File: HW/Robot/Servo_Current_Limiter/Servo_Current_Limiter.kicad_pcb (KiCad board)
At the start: 2 copper layers, 19 parts, among them J1 1x1 2.54mm male, J11 1x2 2.54mm male, J2 1x5 2.54mm male, J3 1x1 2.54mm male, Q1 IRF4905, Q2 BC338, U1 TL071

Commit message: Sch update.
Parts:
- removed C2: 100n, For_Rasterboard:C_Disc_D3.0mm_W1.6mm_Pinf
- added J10: 1x3 2.54mm male, Connector_PinHeader_2.54mm:PinHeader_1x03_P2.54mm_Vertical, F.Cu at (170.4, 50.4)
- added J11: 1x1 2.54mm male, Connector_PinHeader_2.54mm:PinHeader_1x01_P2.54mm_Vertical, F.Cu at (240.0, 28.4)
- added J12: 1x1 2.54mm male, Connector_PinHeader_2.54mm:PinHeader_1x01_P2.54mm_Vertical, F.Cu at (169.0, 38.1)
- added J13: 1x3 2.54mm male, Connector_PinHeader_2.54mm:PinHeader_1x03_P2.54mm_Vertical, F.Cu at (170.4, 28.4)
- added J14: 1x1 2.54mm male, Connector_PinHeader_2.54mm:PinHeader_1x01_P2.54mm_Vertical, F.Cu at (203.3, 50.4)
- added J4: 1x3 2.54mm male, Connector_PinHeader_2.54mm:PinHeader_1x03_P2.54mm_Vertical, F.Cu at (188.0, 139.7)
- added J6: 1x1 2.54mm male, Connector_PinHeader_2.54mm:PinHeader_1x01_P2.54mm_Vertical, F.Cu at (205.7, 38.1)
- added J7: 1x3 2.54mm male, Connector_PinHeader_2.54mm:PinHeader_1x03_P2.54mm_Vertical, F.Cu at (207.2, 28.4)
- added J8: 1x1 2.54mm male, Connector_PinHeader_2.54mm:PinHeader_1x01_P2.54mm_Vertical, F.Cu at (238.5, 53.5)
- added J9: 1x1 2.54mm male, Connector_PinHeader_2.54mm:PinHeader_1x01_P2.54mm_Vertical, F.Cu at (169.0, 60.1)
- added JP1: 1x2 2.54mm male, Connector_PinHeader_2.54mm:PinHeader_1x02_P2.54mm_Vertical, F.Cu at (119.4, 129.5)
- added Q3: IRF4905, Package_TO_SOT_THT:TO-220-3_Vertical, F.Cu at (196.5, 30.0)
- added Q4: BC338, For_Rasterboard:TO-92_Inline_inf, F.Cu at (194.8, 35.3)
- added Q5: IRF4905, Package_TO_SOT_THT:TO-220-3_Vertical, F.Cu at (159.8, 52.0)
- added Q6: BC338, For_Rasterboard:TO-92_Inline_inf, F.Cu at (158.1, 57.3)
- added Q7: IRF4905, Package_TO_SOT_THT:TO-220-3_Vertical, F.Cu at (159.8, 30.0)
- added Q8: BC338, For_Rasterboard:TO-92_Inline_inf, F.Cu at (158.1, 35.3)
- added R10: 10k, For_Rasterboard:R_Axial_DIN0207_L6.3mm_D2.5mm_P7.62mm_Horizontal, F.Cu at (227.0, 65.3)
- added R11: 10k, For_Rasterboard:R_Axial_DIN0207_L6.3mm_D2.5mm_P7.62mm_Horizontal, F.Cu at (227.0, 53.2)
- added R12: 100k, For_Rasterboard:R_Axial_DIN0207_L6.3mm_D2.5mm_P2.54mm_Vertical, F.Cu at (227.0, 57.2)
- added R13: 220, For_Rasterboard:R_Axial_DIN0207_L6.3mm_D2.5mm_Pinf_Horizontal, F.Cu at (157.5, 61.9)
- added R14: 0.1, Resistor_THT:R_Axial_DIN0207_L6.3mm_D2.5mm_P10.16mm_Horizontal, F.Cu at (144.2, 61.9)
- added R15: 100k, For_Rasterboard:R_Axial_DIN0207_L6.3mm_D2.5mm_Pinf_Horizontal, F.Cu at (228.5, 36.2)
- added R16: 10k, For_Rasterboard:R_Axial_DIN0207_L6.3mm_D2.5mm_P7.62mm_Horizontal, F.Cu at (228.5, 40.2)
- added R17: 10k, For_Rasterboard:R_Axial_DIN0207_L6.3mm_D2.5mm_P7.62mm_Horizontal, F.Cu at (228.5, 28.1)
- added R18: 100k, For_Rasterboard:R_Axial_DIN0207_L6.3mm_D2.5mm_P2.54mm_Vertical, F.Cu at (228.5, 32.1)
- added R19: 220, For_Rasterboard:R_Axial_DIN0207_L6.3mm_D2.5mm_Pinf_Horizontal, F.Cu at (157.5, 40.0)
- added R20: 0.1, Resistor_THT:R_Axial_DIN0207_L6.3mm_D2.5mm_P10.16mm_Horizontal, F.Cu at (144.2, 40.0)
- added R21: 100k, For_Rasterboard:R_Axial_DIN0207_L6.3mm_D2.5mm_Pinf_Horizontal, F.Cu at (191.8, 58.2)
- added R22: 10k, For_Rasterboard:R_Axial_DIN0207_L6.3mm_D2.5mm_P7.62mm_Horizontal, F.Cu at (191.8, 62.2)
- added R23: 10k, For_Rasterboard:R_Axial_DIN0207_L6.3mm_D2.5mm_P7.62mm_Horizontal, F.Cu at (191.8, 50.1)
- added R24: 100k, For_Rasterboard:R_Axial_DIN0207_L6.3mm_D2.5mm_P2.54mm_Vertical, F.Cu at (191.8, 54.1)
- added R8: 0.1, Resistor_THT:R_Axial_DIN0207_L6.3mm_D2.5mm_P10.16mm_Horizontal, F.Cu at (180.9, 40.0)
- added R9: 100k, For_Rasterboard:R_Axial_DIN0207_L6.3mm_D2.5mm_Pinf_Horizontal, F.Cu at (227.0, 61.3)
- added RV3: 250, Potentiometer_THT:Potentiometer_Piher_PT-10-V10_Vertical, F.Cu at (144.6, 56.6)
- added RV4: 250, Potentiometer_THT:Potentiometer_Piher_PT-10-V10_Vertical, F.Cu at (144.6, 34.6)
- C1: footprint For_Rasterboard:C_Disc_D3.0mm_W1.6mm_Pinf -> For_Rasterboard:C_Disc_D3.0mm_W1.6mm_P5.00mm
- J2: value 1x5 2.54mm male -> Conn_02x05_Odd_Even; footprint Connector_PinSocket_2.54mm:PinSocket_1x05_P2.54mm_Vertical -> Connector_PinSocket_2.54mm:PinSocket_2x05_P2.54mm_Vertical
- R3: value 220k -> 100k; footprint For_Rasterboard:R_Axial_DIN0207_L6.3mm_D2.5mm_Pinf_Horizontal -> For_Rasterboard:R_Axial_DIN0207_L6.3mm_D2.5mm_P7.62mm_Horizontal
- R4: value 220k -> 10k; footprint For_Rasterboard:R_Axial_DIN0207_L6.3mm_D2.5mm_P7.62mm_Horizontal -> For_Rasterboard:R_Axial_DIN0207_L6.3mm_D2.5mm_P5.08mm_Vertical
- R5: value 220k -> 10k
- R6: value 220k -> 100k; footprint For_Rasterboard:R_Axial_DIN0207_L6.3mm_D2.5mm_Pinf_Horizontal -> For_Rasterboard:R_Axial_DIN0207_L6.3mm_D2.5mm_P2.54mm_Vertical
- R7: value 1k5 -> 220; footprint For_Rasterboard:R_Axial_DIN0207_L6.3mm_D2.5mm_P5.08mm_Vertical -> For_Rasterboard:R_Axial_DIN0207_L6.3mm_D2.5mm_Pinf_Horizontal
- RV2: value 100k -> 250; footprint Potentiometer_THT:Potentiometer_Piher_PT-10-H01_Horizontal -> Potentiometer_THT:Potentiometer_Piher_PT-10-V10_Vertical
- U1: value TL071 -> LM324; footprint Package_DIP:DIP-8_W7.62mm -> Package_DIP:DIP-14_W7.62mm
- moved J2 125.3 mm to (33.0, 162.6)
- moved R7 75.3 mm to (194.2, 40.0)
- moved C1 69.7 mm to (139.7, 139.7)
- moved RV2 68.9 mm to (181.3, 34.6)
- moved U1 46.5 mm to (210.8, 142.2)
- moved Q1 43.4 mm to (193.0, 134.6), turned to -90 degrees
- moved RV1 38.6 mm to (177.8, 132.0)
- moved Q2 35.7 mm to (182.9, 137.2), turned to 90 degrees
- moved R1 34.6 mm to (175.3, 142.2), turned to 90 degrees
- moved R5 31.3 mm to (200.7, 144.8), turned to 90 degrees
- moved R6 30.9 mm to (205.7, 142.2), turned to -90 degrees
- moved R2 26.3 mm to (165.1, 129.5), turned to -90 degrees
- moved R3 22.2 mm to (203.2, 139.7), turned to -90 degrees
- moved R4 20.2 mm to (195.6, 142.2), turned to -90 degrees
- moved J5 17.7 mm to (198.1, 142.2)
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- renumbered J11 to J1, J1 to J3, J3 to J5
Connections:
- net /ch0/sub/op/IN+ renamed Net-(R3-Pad2)
- net /ch0/sub/op/IN- renamed Net-(R5-Pad1)
- A1 pad 10: unconnected-(A1-Pad10) -> /OUT1
- A1 pad 11: unconnected-(A1-Pad11) -> /OUT2
- A1 pad 12: unconnected-(A1-Pad12) -> /OUT3
- A1 pad 17: /DIS0 -> unconnected-(A1-Pad17)
- A1 pad 20: unconnected-(A1-Pad20) -> /ARD_PWM3
- A1 pad 24: unconnected-(A1-Pad24) -> /ARD_PWM2
- A1 pad 25: unconnected-(A1-Pad25) -> /ARD_PWM1
- A1 pad 26: unconnected-(A1-Pad26) -> /ARD_PWM0
- A1 pad 5: +5V -> Net-(A1-Pad5)
- C1 pad 2: GNDA -> GND
- J2 pad 1: unconnected-(J2-Pad1) -> /ARD_PWM0
- J2 pad 2: unconnected-(J2-Pad2) -> /PWM0
- J2 pad 3: /ch0/PWM -> /ARD_PWM1
- J2 pad 4: /ch0/N -> /PWM1
- J2 pad 5: GND -> /ARD_PWM2
- R3 pad 1: GNDA -> GND
- R7 pad 1: Net-(R7-Pad1) -> +5V
- R7 pad 2: GND -> Net-(R7-Pad2)
- RV2 pad 1: Net-(RV2-Pad1) -> Net-(R7-Pad2)
- RV2 pad 2: Net-(R7-Pad1) -> Net-(J6-Pad1)
- RV2 pad 3: Net-(RV2-Pad3) -> GND
- U1 pad 1: Net-(RV2-Pad3) -> /OUT0
- U1 pad 4: GND -> +5V
- U1 pad 5: Net-(RV2-Pad1) -> Net-(R10-Pad2)
- U1 pad 6: /OUT0 -> Net-(R11-Pad1)
- U1 pad 7: +5V -> /OUT1
- U1 pad 8: unconnected-(U1-Pad8) -> /OUT2
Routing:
- net GND: track 0.00 -> 63.5 mm, vias 0 -> 4
- net +5V: track 0.00 -> 43.2 mm, vias 0 -> 4
- net /OUT0: track 0.00 -> 25.4 mm
- net Net-(A1-Pad5): track 0.00 -> 7.62 mm

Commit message: Working.
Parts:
- Q2, Q4, Q6, Q8: value BC338 -> BC548
- R11, R17, R23, R5: footprint For_Rasterboard:R_Axial_DIN0207_L6.3mm_D2.5mm_P7.62mm_Horizontal -> Resistor_THT:R_Axial_DIN0207_L6.3mm_D2.5mm_P10.16mm_Horizontal
- moved Q6 74.5 mm to (227.3, 84.8)
- moved Q8 74.2 mm to (213.4, 84.8)
- moved Q4 67.1 mm to (227.3, 94.0)
- moved R2 29.6 mm to (190.5, 144.8), turned to 90 degrees
- moved Q2 21.6 mm to (198.1, 121.9), turned to -90 degrees
- moved RV1 7.95 mm to (185.3, 134.5), turned to 180 degrees
- moved Q1 2.54 mm to (193.0, 132.1)

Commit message: PCB for 1 channel done.
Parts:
- C1: footprint For_Rasterboard:C_Disc_D3.0mm_W1.6mm_P5.00mm -> For_Rasterboard:C_Disc_D3.0mm_W1.6mm_P2.50mm
- R1: footprint For_Rasterboard:R_Axial_DIN0207_L6.3mm_D2.5mm_Pinf_Horizontal -> For_Rasterboard:R_Axial_DIN0207_L6.3mm_D2.5mm_P5.08mm_Vertical
- R14, R2, R20, R8: footprint Resistor_THT:R_Axial_DIN0207_L6.3mm_D2.5mm_P10.16mm_Horizontal -> For_Rasterboard:R_Axial_DIN0207_L6.3mm_D2.5mm_P7.62mm_Horizontal
- moved R4 133.8 mm to (66.0, 175.3)
- moved R5 133.7 mm to (71.1, 177.8)
- moved J4 131.2 mm to (61.0, 172.7)
- moved Q1 131.2 mm to (66.0, 165.1)
- moved R2 130.6 mm to (63.5, 175.3)
- moved R3 119.0 mm to (88.9, 172.7)
- moved R6 116.5 mm to (94.0, 175.3)
- moved RV1 111.8 mm to (81.2, 175.2), turned to 90 degrees
- moved U1 111.7 mm to (104.1, 175.3)
- moved Q2 109.4 mm to (96.5, 162.6)
- moved J5 106.8 mm to (96.5, 175.3)
- moved J3 95.4 mm to (86.4, 165.1)
- moved R1 93.2 mm to (86.4, 170.2), turned to -90 degrees
- moved C1 43.2 mm to (109.2, 170.2), turned to -90 degrees
- moved J2 25.4 mm to (53.3, 177.8)
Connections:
- A1 pad 17: unconnected-(A1-Pad17) -> /DIS0
- J2 pad 1: /ARD_PWM0 -> /PWM0
- J2 pad 2: /PWM0 -> /ARD_PWM0
- J2 pad 3: /ARD_PWM1 -> /PWM1
- J2 pad 4: /PWM1 -> /ARD_PWM1
- J2 pad 5: /ARD_PWM2 -> /PWM2
- J2 pad 6: /PWM2 -> /ARD_PWM2
- J2 pad 7: /ARD_PWM3 -> /PWM3
- J2 pad 8: /PWM3 -> /ARD_PWM3
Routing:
- net /ARD_PWM1: track 0.00 -> 73.7 mm, vias 0 -> 2
- net /ARD_PWM0: track 0.00 -> 68.6 mm, vias 0 -> 2
- net /OUT1: track 0.00 -> 63.5 mm, vias 0 -> 2
- net /DIS0: track 0.00 -> 53.3 mm, vias 0 -> 3
- net /OUT0: track 25.4 -> 68.6 mm, vias 0 -> 5
- net +5V: track 43.2 -> 86.4 mm, vias 4 -> 2
- net Net-(R3-Pad2): track 0.00 -> 38.2 mm
- net Net-(R5-Pad1): track 0.00 -> 33.0 mm
- net GND: track 63.5 -> 86.3 mm, vias 4 -> 2
- net Net-(J3-Pad1): track 0.00 -> 20.4 mm, vias 0 -> 1
- net /ch0/P: track 0.00 -> 7.62 mm
- net /PWM0: track 0.00 -> 7.62 mm
- net Net-(R1-Pad2): track 0.00 -> 5.15 mm
- net /ch0/N: track 0.00 -> 5.00 mm

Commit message: Correction.
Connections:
- Q2 pad 2: /OUT0 -> Net-(J3-Pad1)
- Q2 pad 3: Net-(J3-Pad1) -> /OUT0
- Q4 pad 2: /OUT1 -> Net-(J6-Pad1)
- Q4 pad 3: Net-(J6-Pad1) -> /OUT1
- Q6 pad 2: /OUT2 -> Net-(J9-Pad1)
- Q6 pad 3: Net-(J9-Pad1) -> /OUT2
- Q8 pad 2: /OUT3 -> Net-(J12-Pad1)
- Q8 pad 3: Net-(J12-Pad1) -> /OUT3
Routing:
- net Net-(J3-Pad1): track 20.4 -> 17.8 mm
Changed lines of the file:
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@@
       (net 46 "/DIS1") (pinfunction "C") (pintype "passive"))
     (pad "2" smd rect locked (at 2.54 0) (size 2 2) (layers "F.Cu" "F.Paste" "F.Mask")
-      (net 22 "/OUT1") (pinfunction "B") (pintype "input"))
+      (net 62 "Net-(J6-Pad1)") (pinfunction "B") (pintype "input"))
     (pad "3" smd rect locked (at 5.08 0) (size 2 2) (layers "F.Cu" "F.Paste" "F.Mask")
-      (net 62 "Net-(J6-Pad1)") (pinfunction "E") (pintype "passive"))
+      (net 22 "/OUT1") (pinfunction "E") (pintype "passive"))
     (model "${KISYS3DMOD}/Package_TO_SOT_THT.3dshapes/TO-92_Inline_Wide.wrl"
       (offset (xyz 0 0 0))
@@
       (net 48 "/DIS2") (pinfunction "C") (pintype "passive"))
     (pad "2" smd rect locked (at 2.54 0) (size 2 2) (layers "F.Cu" "F.Paste" "F.Mask")
-      (net 23 "/OUT2") (pinfunction "B") (pintype "input"))
+      (net 63 "Net-(J9-Pad1)") (pinfunction "B") (pintype "input"))
     (pad "3" smd rect locked (at 5.08 0) (size 2 2) (layers "F.Cu" "F.Paste" "F.Mask")
-      (net 63 "Net-(J9-Pad1)") (pinfunction "E") (pintype "passive"))
+      (net 23 "/OUT2") (pinfunction "E") (pintype "passive"))
     (model "${KISYS3DMOD}/Package_TO_SOT_THT.3dshapes/TO-92_Inline_Wide.wrl"
       (offset (xyz 0 0 0))
@@
       (net 50 "/DIS3") (pinfunction "C") (pintype "passive"))
     (pad "2" smd rect locked (at 2.54 0) (size 2 2) (layers "F.Cu" "F.Paste" "F.Mask")
-      (net 33 "/OUT3") (pinfunction "B") (pintype "input"))
+      (net 43 "Net-(J12-Pad1)") (pinfunction "B") (pintype "input"))
     (pad "3" smd rect locked (at 5.08 0) (size 2 2) (layers "F.Cu" "F.Paste" "F.Mask")
-      (net 43 "Net-(J12-Pad1)") (pinfunction "E") (pintype "passive"))
+      (net 33 "/OUT3") (pinfunction "E") (pintype "passive"))
     (model "${KISYS3DMOD}/Package_TO_SOT_THT.3dshapes/TO-92_Inline_Wide.wrl"
       (offset (xyz 0 0 0))
@@
       (net 6 "/DIS0") (pinfunction "C") (pintype "passive"))
     (pad "2" smd rect locked (at 2.54 0 270) (size 2 2) (layers "F.Cu" "F.Paste" "F.Mask")
-      (net 1 "/OUT0") (pinfunction "B") (pintype "input"))
+      (net 61 "Net-(J3-Pad1)") (pinfunction "B") (pintype "input"))
     (pad "3" smd rect locked (at 5.08 0 270) (size 2 2) (layers "F.Cu" "F.Paste" "F.Mask")
-      (net 61 "Net-(J3-Pad1)") (pinfunction "E") (pintype "passive"))
+      (net 1 "/OUT0") (pinfunction "E") (pintype "passive"))
     (model "${KISYS3DMOD}/Package_TO_SOT_THT.3dshapes/TO-92_Inline_Wide.wrl"
       (offset (xyz 0 0 0))
@@
     )
   )
-  (segment (start 91.44 165.1) (end 91.44 175.26) (width 2) (layer "F.Cu") (net 1))
-  (segment (start 93.98 165.1) (end 93.98 142.24) (width 2) (layer "F.Cu") (net 1))
+  (segment (start 91.44 167.64) (end 91.44 175.26) (width 2) (layer "F.Cu") (net 1))
+  (segment (start 93.98 167.64) (end 93.98 142.24) (width 2) (layer "F.Cu") (net 1))
   (via (at 91.44 175.26) (size 2) (drill 0.8) (layers "F.Cu" "B.Cu") (net 1))
-  (via (at 91.44 165.1) (size 2) (drill 0.8) (layers "F.Cu" "B.Cu") (net 1))
-  (via (at 93.98 165.1) (size 2) (drill 0.8) (layers "F.Cu" "B.Cu") (net 1))
-  (via (at 96.52 165.1) (size 2) (drill 0.8) (layers "F.Cu" "B.Cu") (net 1))
+  (via (at 91.44 167.64) (size 2) (drill 0.8) (layers "F.Cu" "B.Cu") (net 1))
+  (via (at 93.98 167.64) (size 2) (drill 0.8) (layers "F.Cu" "B.Cu") (net 1))
+  (via (at 96.52 167.64) (size 2) (drill 0.8) (layers "F.Cu" "B.Cu") (net 1))
   (via (at 93.98 142.24) (size 2) (drill 0.8) (layers "F.Cu" "B.Cu") (net 1))
   (segment (start 91.44 175.26) (end 104.14 175.26) (width 2) (layer "B.Cu") (net 1))
   (segment (start 93.98 142.24) (end 111.76 142.24) (width 2) (layer "B.Cu") (net 1))
-  (segment (start 91.44 165.1) (end 96.52 165.1) (width 2) (layer "B.Cu") (net 1))
+  (segment (start 91.44 167.64) (end 96.52 167.64) (width 2) (layer "B.Cu") (net 1))
   (segment (start 71.12 149.86) (end 71.12 162.56) (width 2) (layer "F.Cu") (net 6))
   (via (at 71.12 149.86) (size 2) (drill 0.8) (layers "F.Cu" "B.Cu") (net 6))
@@
   (segment (start 50.8 177.8) (end 48.26 177.8) (width 2) (layer "B.Cu") (net 37))
   (segment (start 60.96 177.8) (end 53.34 177.8) (width 2) (layer "B.Cu") (net 38))
-  (via (at 96.52 167.64) (size 2) (drill 0.8) (layers "F.Cu" "B.Cu") (net 61))
-  (segment (start 86.36 167.64) (end 96.52 167.64) (width 2) (layer "B.Cu") (net 61))
-  (segment (start 86.36 165.1) (end 86.36 167.64) (width 2) (layer "B.Cu") (net 61))
+  (via (at 96.52 165.1) (size 2) (drill 0.8) (layers "F.Cu" "B.Cu") (net 61))
+  (segment (start 86.36 165.1) (end 96.52 165.1) (width 2) (layer "B.Cu") (net 61))
   (segment (start 86.28 165.18) (end 86.36 165.1) (width 2) (layer "B.Cu") (net 61))
   (segment (start 78.74 165.18) (end 86.28 165.18) (width 2) (layer "B.Cu") (net 61))

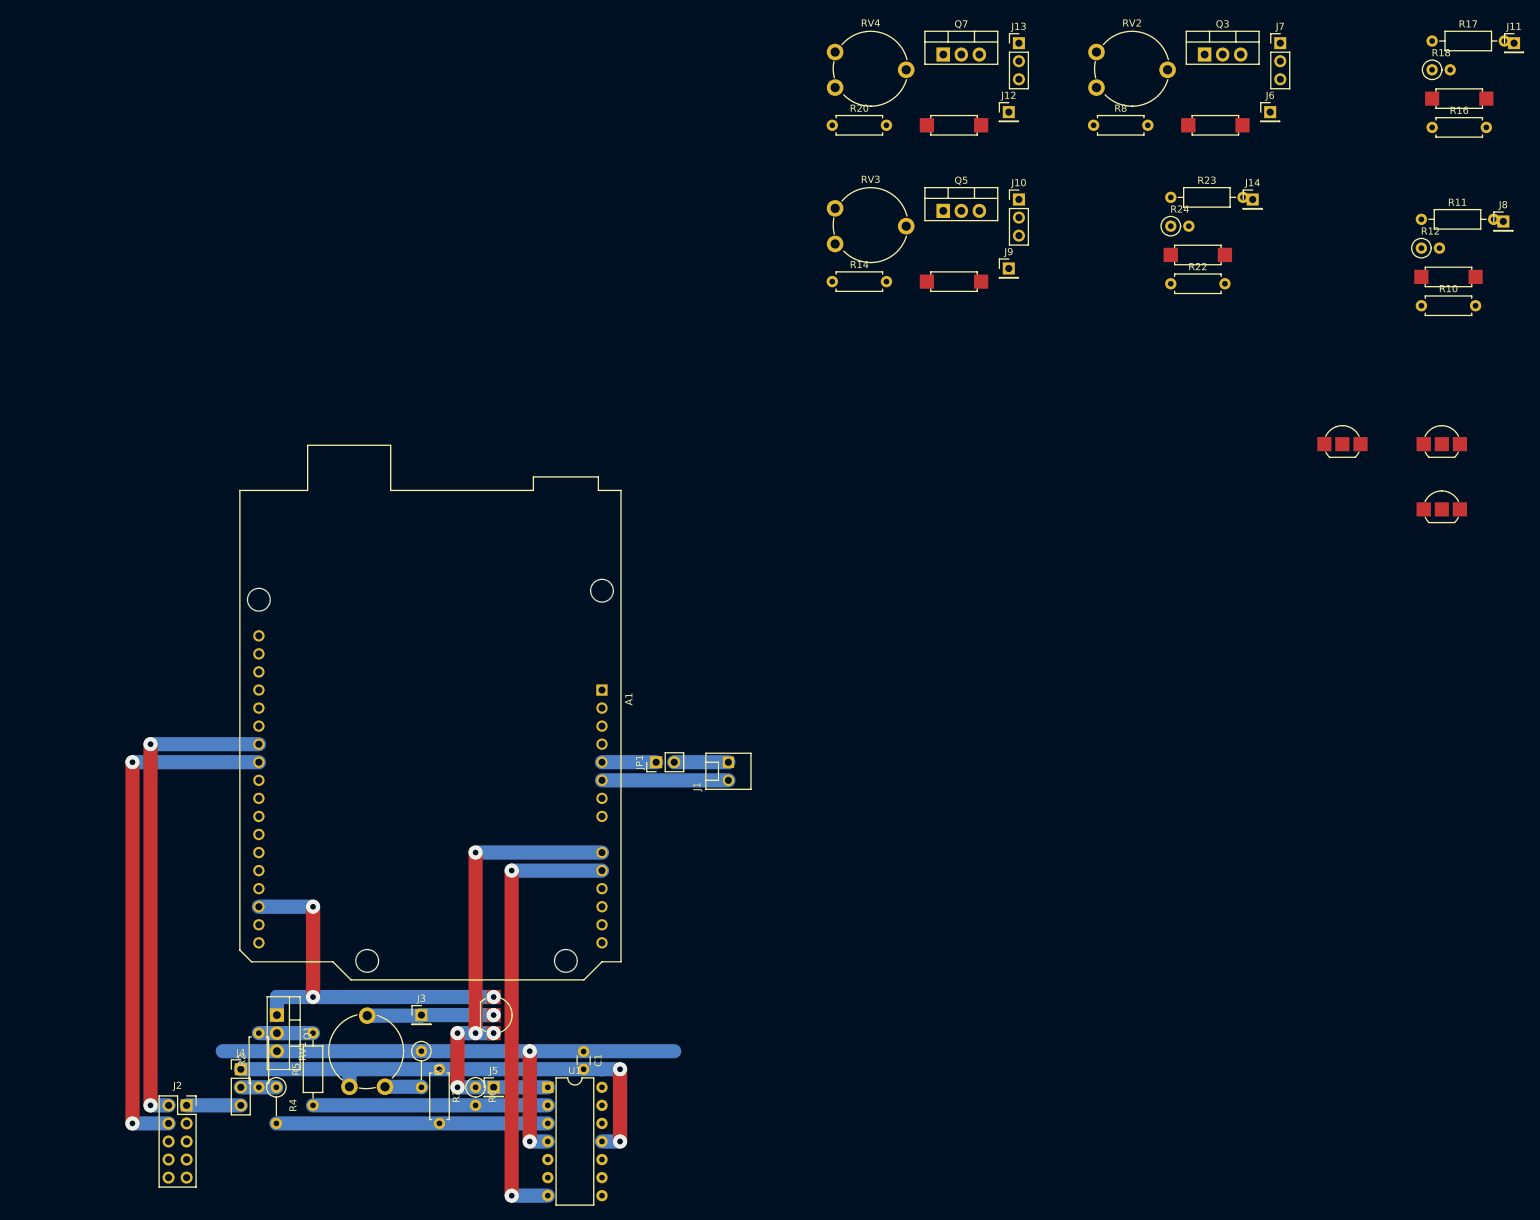
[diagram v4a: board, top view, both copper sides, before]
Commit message: Dual power. Snapped to grid.
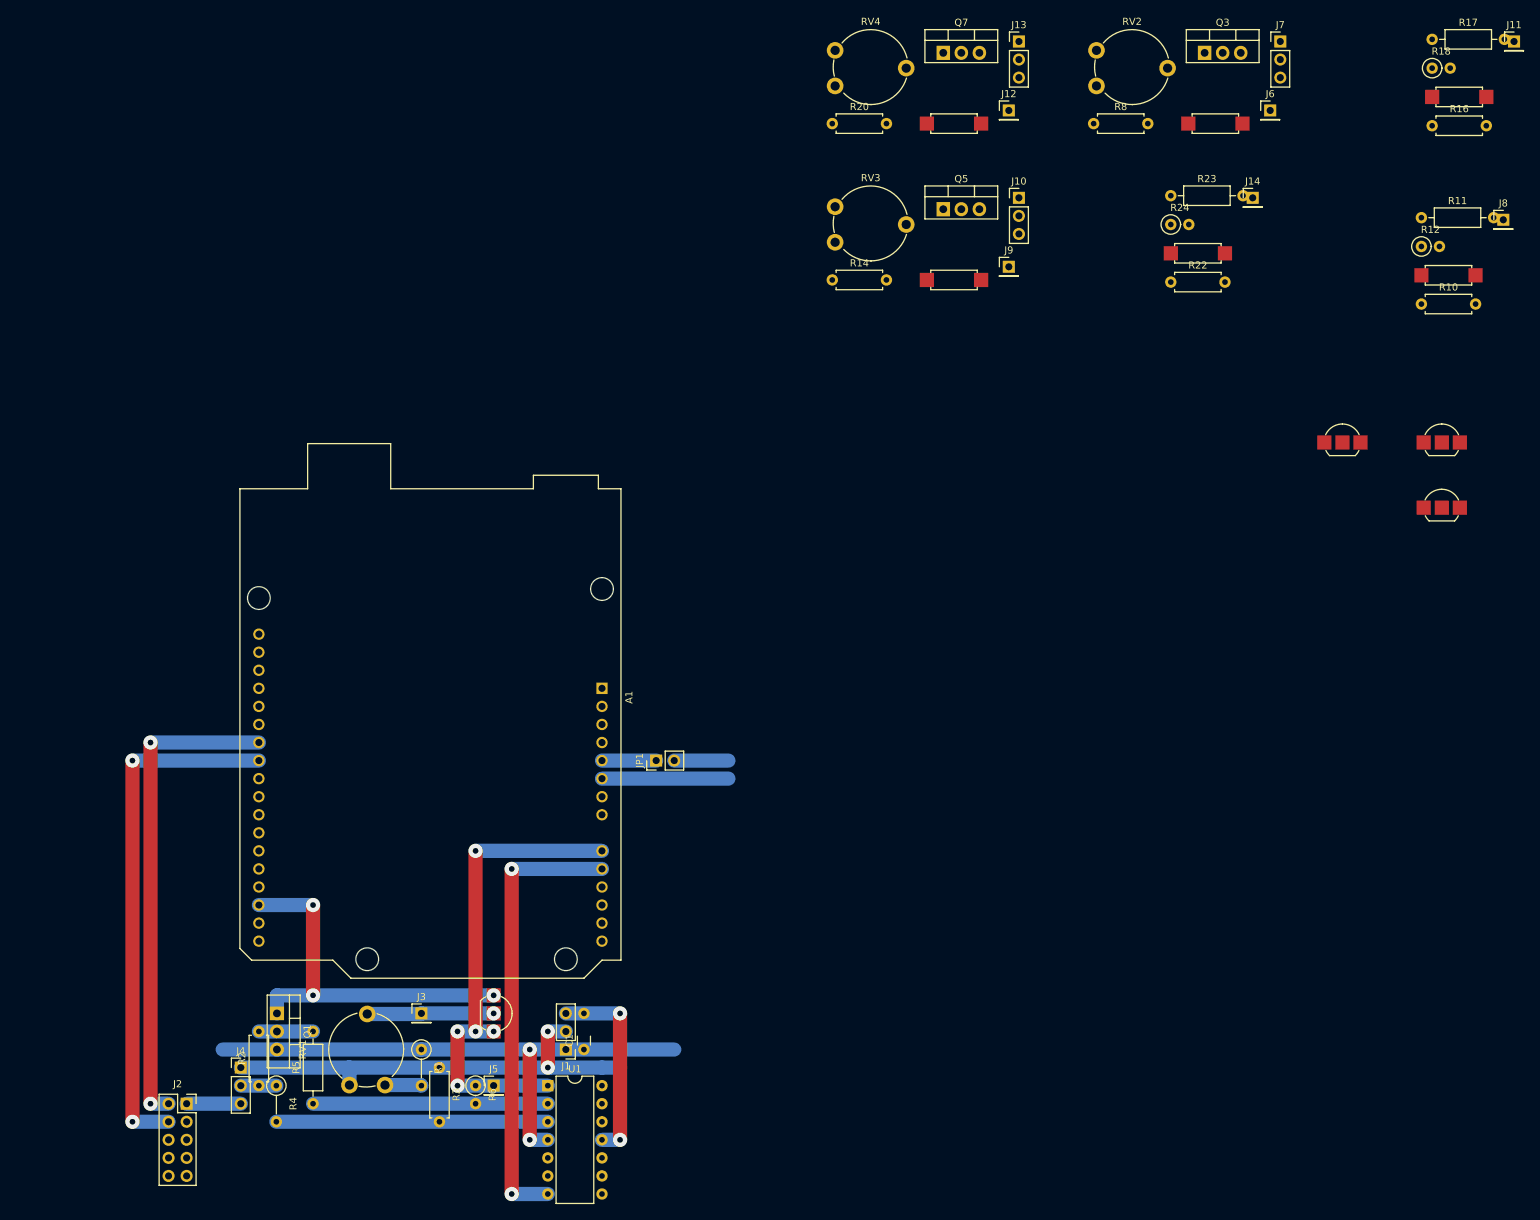
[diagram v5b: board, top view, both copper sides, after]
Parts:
- C1: footprint For_Rasterboard:C_Disc_D3.0mm_W1.6mm_P2.50mm -> For_Rasterboard:C_Disc_D3.0mm_W1.6mm_P5.00mm
- J1: value 1x2 2.54mm male -> 1x3 2.54mm male; footprint Extra_Common:MOLEX-22-23-2021 -> Connector_PinHeader_2.54mm:PinHeader_1x03_P2.54mm_Vertical
- moved J1 45.3 mm to (106.7, 169.9), turned to 180 degrees
- moved C1 0.28 mm to (109.2, 169.9), turned to 90 degrees
- moved J2 0.24 mm to (53.3, 177.6)
- moved Q2 0.24 mm to (96.5, 162.3)
- moved R1 0.24 mm to (86.4, 169.9)
- moved R5 0.24 mm to (71.1, 177.6)
- moved RV1 0.24 mm to (81.2, 174.9)
- moved J9 0.24 mm to (169.0, 59.9)
- moved R23 0.24 mm to (191.8, 49.9)
- moved R17 0.24 mm to (228.5, 27.9)
- moved A1 0.23 mm to (111.8, 119.1)
- moved J10 0.23 mm to (170.4, 50.2)
- moved J11 0.23 mm to (240.0, 28.2)
- moved J12 0.23 mm to (169.0, 37.9)
- moved J13 0.23 mm to (170.4, 28.2)
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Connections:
- C1 pad 2: GND -> -5V
- U1 pad 11: GND -> -5V
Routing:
- net -5V: track 0.00 -> 27.9 mm, vias 0 -> 2
- net GND: track 86.3 -> 81.2 mm
